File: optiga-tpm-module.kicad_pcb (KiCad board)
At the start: 2 copper layers, 20 x 29 mm, 37 parts, among them J1 Plug_Samtec_ERM5_2x20_ERM5-02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, U1 SLB9672XU20FW1624XTMA1

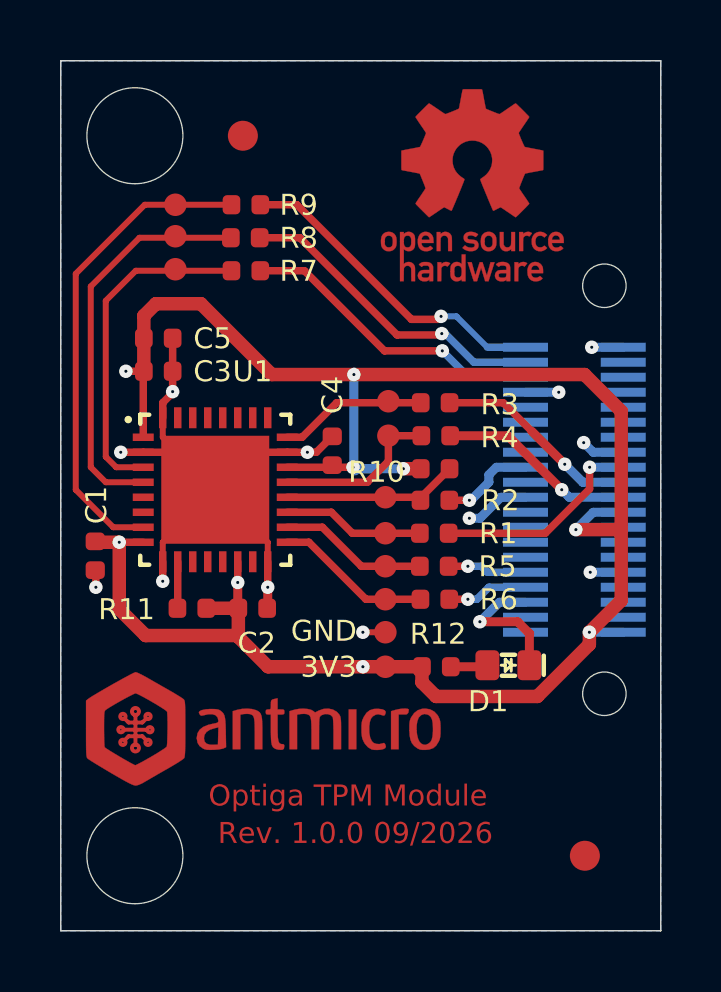
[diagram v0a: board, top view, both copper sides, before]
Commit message: [#104798] Change PCB stackup, clean up vias and traces according to review
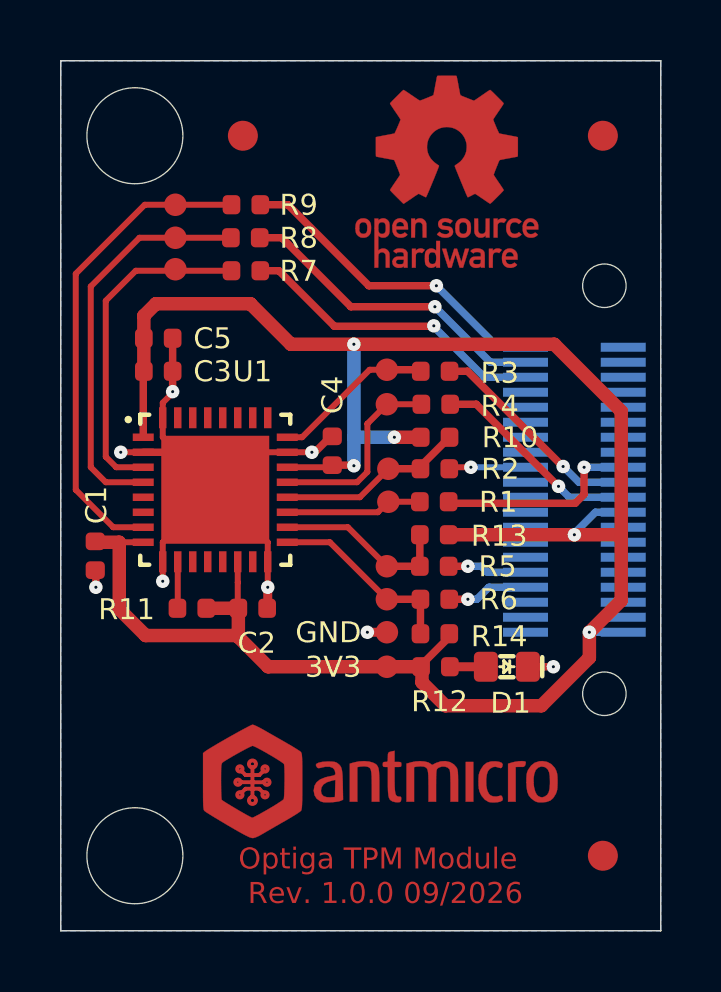
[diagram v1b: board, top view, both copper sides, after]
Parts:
- added FD3: Fiducial_1mm_Mask2mm, antmicro-footprints:Fiducial_1mm_Mask2mm, F.Cu at (346.1, 218.0)
- added R13: R_10k_0402, antmicro-footprints:R_0402_1005Metric, F.Cu at (340.5, 231.3)
- added R14: R_10k_0402, antmicro-footprints:R_0402_1005Metric, F.Cu at (340.5, 234.6)
- moved N1 4.27 mm to (338.6, 239.6)
- moved TP2 1.05 mm to (338.9, 230.2)
- moved TP5 1.05 mm to (338.9, 226.9)
- moved TP4 1.05 mm to (338.9, 225.8)
- moved R1 1.05 mm to (340.5, 230.2)
- moved R2 1.05 mm to (340.5, 229.1)
- moved R3 1.05 mm to (340.5, 225.8)
- moved R4 1.05 mm to (340.5, 226.9)
- moved R10 1.05 mm to (340.5, 228.1)
- moved N2 0.96 mm to (340.9, 219.2)
- moved TP3 0.96 mm to (338.9, 229.1)
- moved FD2 0.60 mm to (346.1, 242.0)
- moved D1 0.07 mm to (342.9, 235.7)
- moved TP9 0.05 mm to (331.9, 221.4)
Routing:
- net GND: track 35.6 -> 24.7 mm, vias 13 -> 8
- net +3V3: track 69.8 -> 75.5 mm, vias 9 -> 5
- net /~{RST}_R: track 5.23 -> 6.38 mm
- net /~{PIRQ}_R: track 4.96 -> 6.01 mm
- net /SPI.MOSI_R: track 5.61 -> 6.49 mm
- net /SPI.~{CS}: track 3.14 -> 2.56 mm
